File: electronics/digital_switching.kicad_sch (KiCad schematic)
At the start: 20 parts, among them J10 CH2, J13 CH3, J14 CH4, J15 CH5, J3 CH1, U10 BTS7006, U6 BTS7006, U7 BTS7006, U8 BTS7006, U9 BTS7006

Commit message: no tracks, but placement looks good
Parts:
- removed J10: CH2, HeavyDuty:keystone_m3_screw_terminal_vertical, symbol Connector_Generic:Conn_01x01
- removed J13: CH3, HeavyDuty:keystone_m3_screw_terminal_vertical, symbol Connector_Generic:Conn_01x01
- removed J14: CH4, HeavyDuty:keystone_m3_screw_terminal_vertical, symbol Connector_Generic:Conn_01x01
- removed J15: CH5, HeavyDuty:keystone_m3_screw_terminal_vertical, symbol Connector_Generic:Conn_01x01
- removed J3: CH1, HeavyDuty:keystone_m3_screw_terminal_vertical, symbol Connector_Generic:Conn_01x01
- added J5: DB12, HeavyDuty:5p_terminal_DB12, symbol Connector_Generic:Conn_01x05
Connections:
- net at U7.10 (OUT), U7.12 (OUT), U7.13 (OUT)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: now also J5.2 (Pin_2)
- net at U6.10 (OUT), U6.12 (OUT), U6.13 (OUT)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: now also J5.1 (Pin_1)
- net at U9.10 (OUT), U9.12 (OUT), U9.13 (OUT)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: now also J5.4 (Pin_4)
- net at U10.10 (OUT), U10.12 (OUT), U10.13 (OUT)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: now also J5.5 (Pin_5)
- net at U8.10 (OUT), U8.12 (OUT), U8.13 (OUT)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: now also J5.3 (Pin_3)

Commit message: nerd weekend update
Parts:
- added D14: APFA3010, LED_SMD:LED_Kingbright_APFA3010_3x1.5mm_Horizontal, symbol LED:APFA3010
- added U21: TCA9555PWR, Package_SO:TSSOP-24_4.4x7.8mm_P0.65mm, symbol Interface_Expansion:TCA9555PWR
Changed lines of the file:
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@@
+	)
+	(symbol
+		(lib_id "LED:APFA3010")
+		(at 251.46 152.4 0)
+		(unit 1)
+		(exclude_from_sim no)
+		(in_bom yes)
+		(on_board yes)
+		(dnp no)
+		(fields_autoplaced yes)
+		(property "Reference" "D14"
+			(at 251.46 138.43 0)
+			(effects
+				(font
+					(size 1.27 1.27)
+				)
+			)
+		)
+		(property "Value" "APFA3010"
+			(at 251.46 140.97 0)
+			(effects
+				(font
+					(size 1.27 1.27)
+				)
+			)
+		)
+		(property "Footprint" "LED_SMD:LED_Kingbright_APFA3010_3x1.5mm_Horizontal"
+			(at 251.46 139.7 0)
+			(effects
+				(font
+					(size 1.27 1.27)
+				)
+				(hide yes)
+			)
+		)
+		(property "Datasheet" "http://www.kingbrightusa.com/images/catalog/SPEC/APFA3010LSEEZGKQBKC.pdf"
+			(at 251.46 163.83 0)
+			(effects
+				(font
+					(size 1.27 1.27)
+				)
+				(hide yes)
+			)
+		)
+		(property "Description" "LED RGB, Common Anode, SMD, 3.0x1.5mm, Horizontal"
+			(at 251.46 152.4 0)
+			(effects
+				(font
+					(size 1.27 1.27)
+				)
+				(hide yes)
+			)
+		)
+		(pin "4"
+		)
+		(pin "1"
+		)
+		(pin "3"
+		)
+		(pin "2"
+		)
+		(instances
+			(project ""
+				(path "/eeb1234c-eae0-4ac6-a30d-2a978d66d889/04c402f1-b99a-4823-99a0-0c7312782f29/3b4f4bb7-bd1f-4bbe-884d-f3621abf4676"
+					(reference "D14")
+					(unit 1)
+				)
+			)
+		)
 	)
 	(symbol
@@
 					(unit 1)
 				)
+			)
+		)
+	)
+	(symbol
+		(lib_id "Interface_Expansion:TCA9555PWR")
+		(at 96.52 110.49 0)
+		(unit 1)
+		(exclude_from_sim no)
+		(in_bom yes)
+		(on_board yes)
+		(dnp no)
+		(fields_autoplaced yes)
+		(property "Reference" "U21"
+			(at 98.7141 82.55 0)
+			(effects
+				(font
+					(size 1.27 1.27)
+				)
+				(justify left)
+			)
+		)
+		(property "Value" "TCA9555PWR"
+			(at 98.7141 85.09 0)
+			(effects
+				(font
+					(size 1.27 1.27)
+				)
+				(justify left)
+			)
+		)
+		(property "Footprint" "Package_SO:TSSOP-24_4.4x7.8mm_P0.65mm"
+			(at 123.19 135.89 0)
+			(effects
+				(font
+					(size 1.27 1.27)
+				)
+				(hide yes)
+			)
+		)
+		(property "Datasheet" "http://www.ti.com/lit/ds/symlink/tca9555.pdf"
+			(at 83.82 87.63 0)
+			(effects
+				(font
+					(size 1.27 1.27)
+				)
+				(hide yes)
+			)
+		)
+		(property "Description" "16-bit I/O expander, I2C and SMBus interface, interrupts, w/ pull-ups, TSSOP-24 package"
+			(at 101.092 152.908 0)
+			(effects
+				(font
+					(size 1.27 1.27)
+				)
+				(hide yes)
+			)
+		)
+		(pin "22"
+		)
+		(pin "5"
+		)
+		(pin "4"
+		)
+		(pin "3"
+		)
+		(pin "24"
+		)
+		(pin "6"
+		)
+		(pin "18"
+		)
+		(pin "10"
+		)
+		(pin "11"
+		)
+		(pin "9"
+		)
+		(pin "13"
+		)
+		(pin "19"
+		)
+		(pin "20"
+		)
+		(pin "21"
+		)
+		(pin "2"
+		)
+		(pin "17"
+		)
+		(pin "1"
+		)
+		(pin "23"
+		)
+		(pin "14"
+		)
+		(pin "15"
+		)
+		(pin "7"
+		)
+		(pin "8"
+		)
+		(pin "16"
+		)
+		(pin "12"
+		)
+		(instances
+			(project "electronics"
+				(path "/eeb1234c-eae0-4ac6-a30d-2a978d66d889/04c402f1-b99a-4823-99a0-0c7312782f29/3b4f4bb7-bd1f-4bbe-884d-f3621abf4676"
+					(reference "U21")
+					(unit 1)
+				)

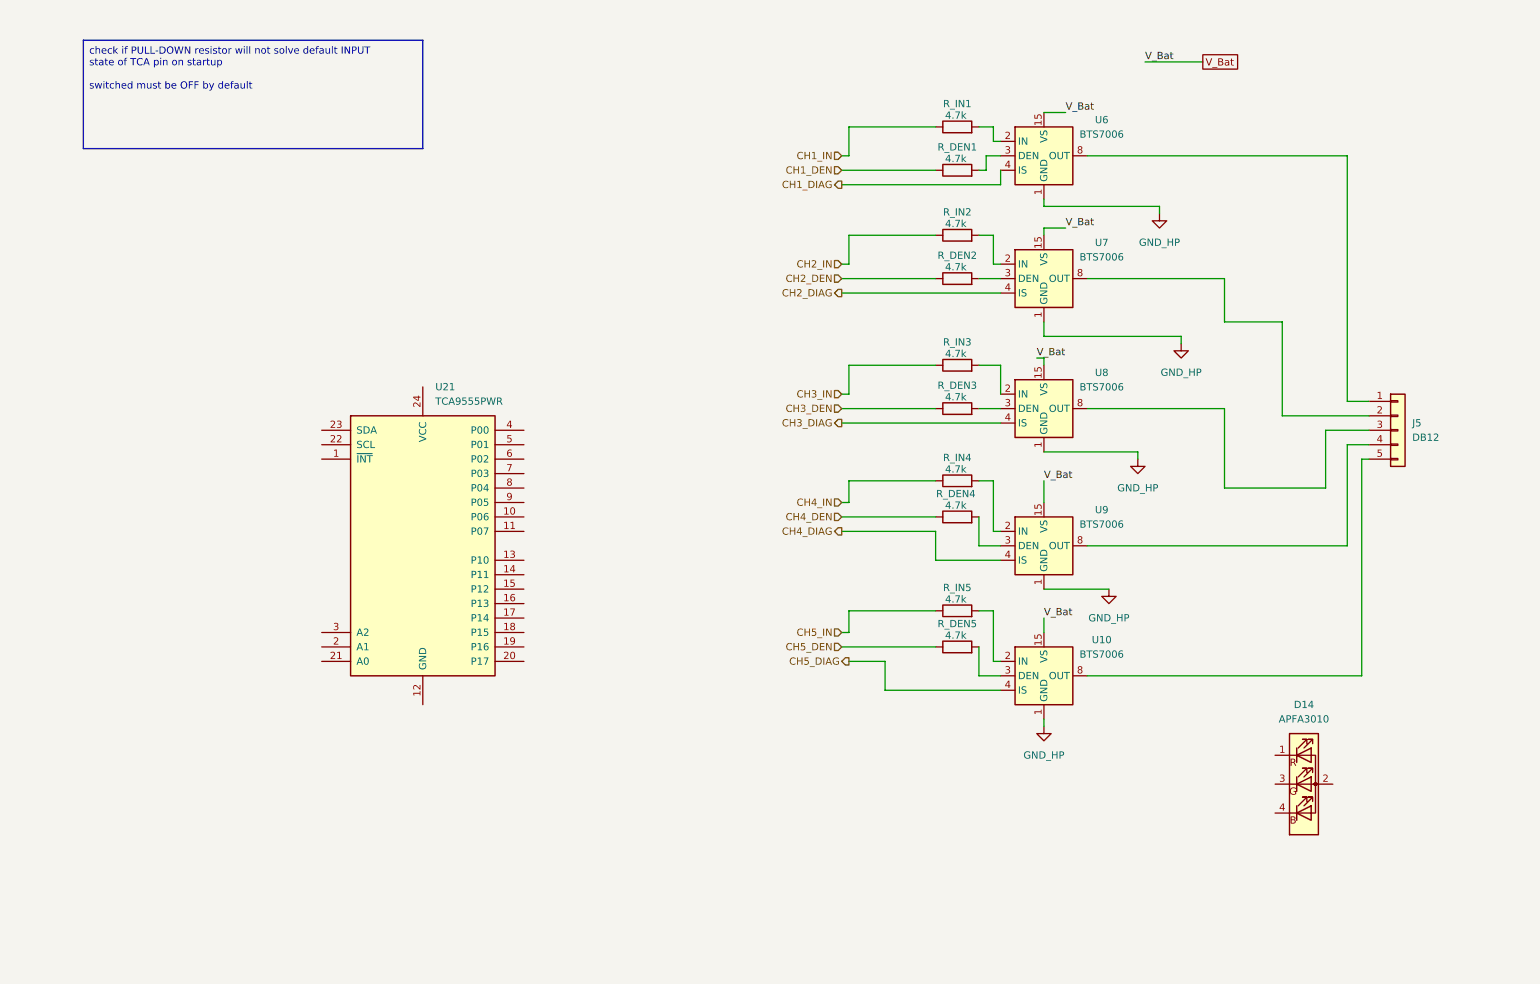
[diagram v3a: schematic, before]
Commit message: start to create BOM and finalising symbol fields
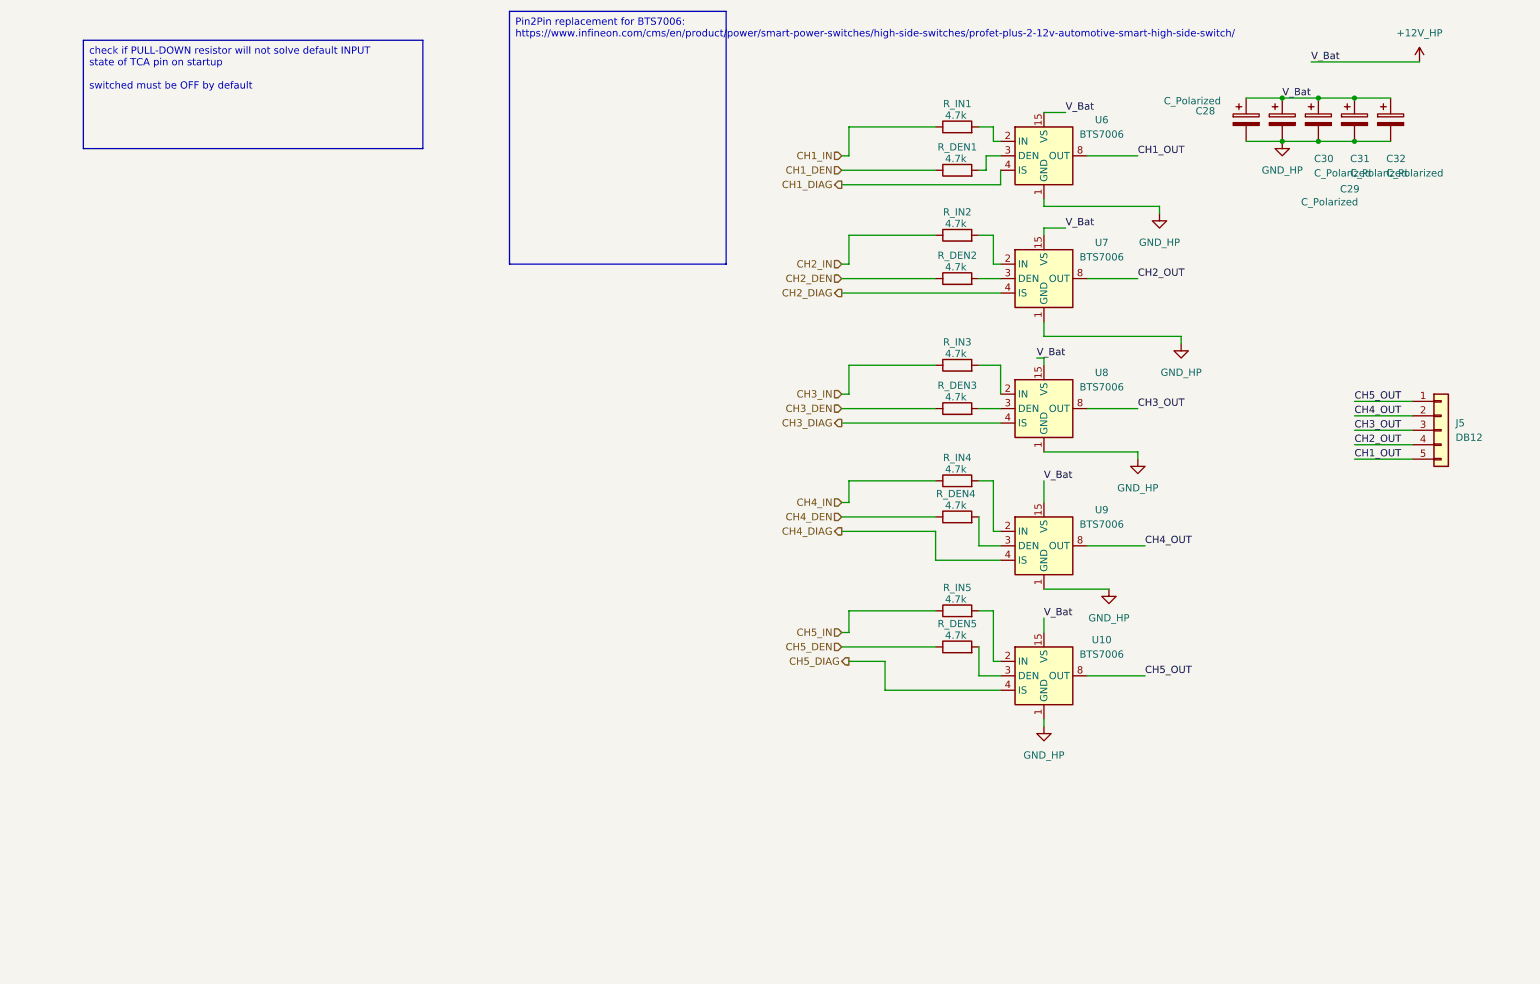
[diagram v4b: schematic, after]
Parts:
- removed D14: APFA3010, LED_SMD:LED_Kingbright_APFA3010_3x1.5mm_Horizontal, symbol LED:APFA3010
- removed U21: TCA9555PWR, Package_SO:TSSOP-24_4.4x7.8mm_P0.65mm, symbol Interface_Expansion:TCA9555PWR
- added C28, C29, C30, C31, C32: C_Polarized, Capacitor_THT:CP_Radial_D5.0mm_P2.50mm, symbol Device:C_Polarized
- J5: LCSCc (none) -> C2927513
- R_DEN1, R_DEN2, R_DEN3, R_DEN4, R_DEN5, R_IN1, R_IN2, R_IN3, R_IN4, R_IN5: footprint Resistor_SMD:R_0805_2012Metric_Pad1.20x1.40mm_HandSolder -> Resistor_SMD:R_0805_2012Metric
- U6: Manufacturer (none) -> Infineon; Mfr Part (none) -> BTS7006-1EPP; Mouser (none) -> 726-BTS70061EPPXUMA1
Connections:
- net GND_HP: now also C28.2, C29.2, C30.2, C31.2, C32.2
- net CH2_OUT: now reaches U7.10 (OUT), U7.12 (OUT), U7.13 (OUT), U7.14 (OUT), U7.8 (OUT), U7.9 (OUT)
- net CH2_OUT: now also J5.4 (Pin_4); no longer J5.2 (Pin_2)
- net CH1_OUT: now reaches U6.10 (OUT), U6.12 (OUT), U6.13 (OUT), U6.14 (OUT), U6.8 (OUT), U6.9 (OUT)
- net CH1_OUT: now also J5.5 (Pin_5); no longer J5.1 (Pin_1)
- net CH4_OUT: now reaches U9.10 (OUT), U9.12 (OUT), U9.13 (OUT), U9.14 (OUT), U9.8 (OUT), U9.9 (OUT)
- net CH4_OUT: now also J5.2 (Pin_2); no longer J5.4 (Pin_4)
- net CH3_OUT: now reaches J5.3 (Pin_3), U8.10 (OUT), U8.12 (OUT), U8.13 (OUT), U8.14 (OUT), U8.8 (OUT), U8.9 (OUT)
- net CH5_OUT: now reaches U10.10 (OUT), U10.12 (OUT), U10.13 (OUT), U10.14 (OUT), U10.8 (OUT), U10.9 (OUT)
- net CH5_OUT: now also J5.1 (Pin_1); no longer J5.5 (Pin_5)
- net V_Bat renamed +12V_HP
- net +12V_HP: now also C28.1, C29.1, C30.1, C31.1, C32.1

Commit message: layouting progress. some 3d models upload
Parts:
- added C_SENSE1, C_SENSE2, C_SENSE3, C_SENSE4: 220pF, Capacitor_SMD:C_0805_2012Metric, symbol Device:C_Small
- added C_SENSE5: 220pF, Capacitor_SMD:C_1210_3225Metric_Pad1.33x2.70mm_HandSolder, symbol Device:C_Small
- added R_ADC1, R_ADC2, R_ADC3, R_ADC4, R_ADC5: 4.7k, Resistor_SMD:R_0805_2012Metric, symbol Device:R
- added R_SENSE1, R_SENSE2, R_SENSE3, R_SENSE4, R_SENSE5: 1.2k, Resistor_SMD:R_0805_2012Metric, symbol Device:R
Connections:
- net CH1_DIAG: now also C_SENSE1.1, R_ADC1.1; no longer U6.4 (IS)
- net CH2_DIAG: now also C_SENSE2.1, R_ADC2.1; no longer U7.4 (IS)
- net CH3_DIAG: now also C_SENSE3.1, R_ADC3.1; no longer U8.4 (IS)
- net CH4_DIAG: now also C_SENSE4.1, R_ADC4.1; no longer U9.4 (IS)
- net CH5_DIAG: now also C_SENSE5.1, R_ADC5.1; no longer U10.4 (IS)
- new net GND_LP: C_SENSE1.2, C_SENSE2.2, C_SENSE3.2, C_SENSE4.2, C_SENSE5.2, R_SENSE1.1, R_SENSE2.1, R_SENSE3.1, R_SENSE4.1, R_SENSE5.1
- new net ch1_sense: R_ADC1.2, R_SENSE1.2, U6.4 (IS)
- new net ch2_sense: R_ADC2.2, R_SENSE2.2, U7.4 (IS)
- new net ch3_sense: R_ADC3.2, R_SENSE3.2, U8.4 (IS)
- new net ch4_sense: R_ADC4.2, R_SENSE4.2, U9.4 (IS)
- new net ch5_sense: R_ADC5.2, R_SENSE5.2, U10.4 (IS)
